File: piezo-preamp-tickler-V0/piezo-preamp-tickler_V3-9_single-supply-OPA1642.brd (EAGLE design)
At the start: 100 x 20 mm, 61 parts, among them IC1 OPA1642, IC2 MCP73831, IC3 QS6K1, IC4 BQ297X, IC5 SC4503, IC6 TPS7A49, J1 HEADPHONES, J2 PHONE, J3 Mixer, J5 Battery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

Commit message: resolved cosmetic issues in mems and piezo for 5k and 50k resistor values that should be 4.7k and 47K
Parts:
- R13: value 5k -> 4.7K
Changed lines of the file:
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@@
 <attribute name="VALUE" x="72.797" y="12.941" size="0.6604" layer="27" font="vector" ratio="15" rot="R180"/>
 </element>
-<element name="R13" library="CMU-ArtFab" package="R0603" value="5k" x="65.375" y="10.115" smashed="yes">
+<element name="R13" library="CMU-ArtFab" package="R0603" value="4.7K" x="65.375" y="10.115" smashed="yes">
 <attribute name="NAME" x="66.14" y="11.405" size="0.6604" layer="25" font="vector" ratio="15" rot="R180"/>
 <attribute name="VALUE" x="64.65" y="8.771" size="0.6604" layer="27" font="vector" ratio="15"/>

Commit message: capacitors renumbered in sequence
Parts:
- C10: value 2.2pF -> 56nF
- C11: value 68uF -> 2.2pF; device rcl:C1206 -> rcl:C0603
- C12: value 10uF -> 68uF; device rcl:C0603 -> rcl:C1206
- C13: value 10nF -> 10uF
- C15: value 10uF -> 10nF
- C16: value 4.7uF -> 10uF
- C7: value 0.1uF -> 4.7uF
- C8: value 10uF -> 0.1uF
- C9: value 56nF -> 10uF
- moved C9 29.1 mm to (47.4, 11.6)
- moved C11 28.4 mm to (79.2, 6.31), turned to 0 degrees
- moved C8 28.1 mm to (75.0, 6.30)
- moved C12 18.5 mm to (52.3, 15.2)
- moved C7 16.0 mm to (59.1, 7.80)
- moved C16 13.9 mm to (68.6, 18.0), turned to 180 degrees
- moved C14 13.1 mm to (70.5, 6.32), turned to 180 degrees
- moved C13 6.49 mm to (65.5, 2.23)
- moved C10 5.83 mm to (75.0, 2.32)
- moved C15 3.98 mm to (64.6, 18.0), turned to 0 degrees
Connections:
- net +12V: now also C14.1; no longer C12.1
- net BATGND: now also C8.1; no longer C7.1
- net GND: now also C10.2, C13.2, C16.2; no longer C11.2, C14.2, C8.2
- net N$26: now also C14.2; no longer C13.2
- net N$28: now also C15.1; no longer C14.1
- net N$29: now also C10.1; no longer C9.1
- net N$30: now also C11.2; no longer C10.2
- net N$42: now also C8.2; no longer C7.2
- net USBGND: now also C7.2; no longer C16.2
- net V+: now also C12.1, C16.1; no longer C10.1, C15.1
- net VBAT: now also C7.1, C9.1; no longer C16.1, C8.1

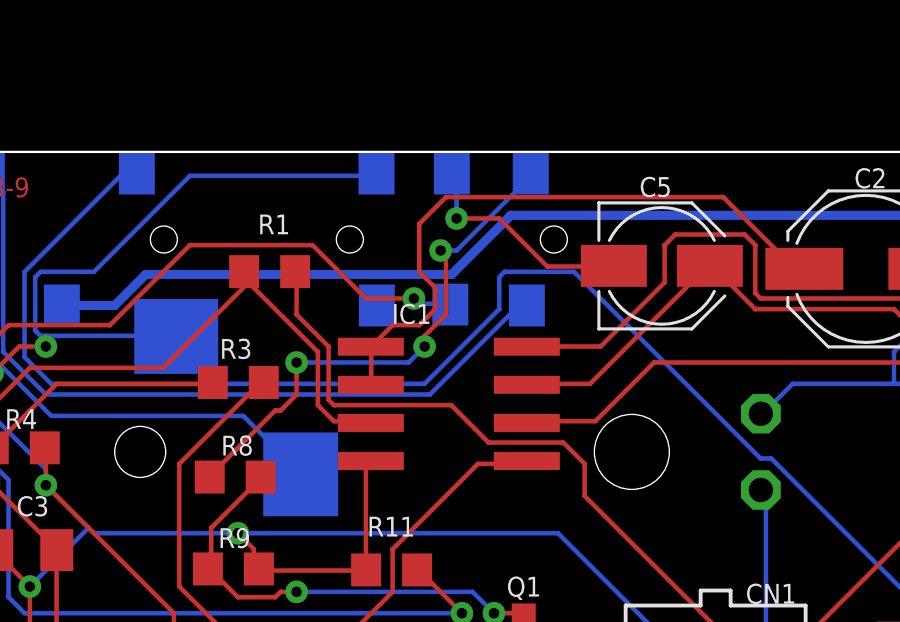
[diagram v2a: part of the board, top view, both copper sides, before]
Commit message: OPA1642 device added from CMU artfab library
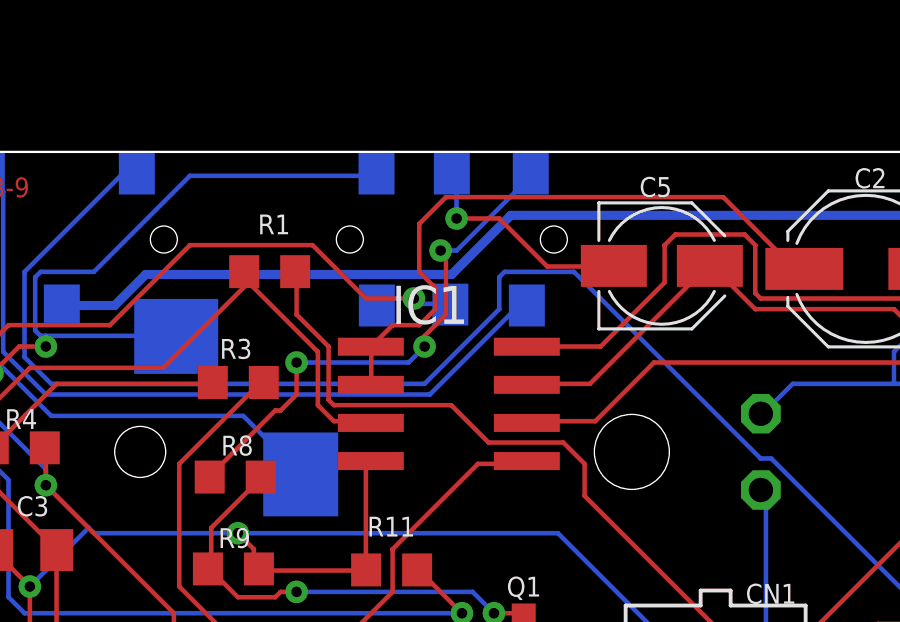
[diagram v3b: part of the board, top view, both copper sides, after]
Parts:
- IC1: device linear:SO08 -> CMU-ArtFab:SO08
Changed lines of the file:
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@@
 <attribute name="VALUE" x="58.065" y="6.495" size="0.6604" layer="27" font="vector" ratio="15"/>
-</element>
-<element name="IC1" library="linear" library_urn="urn:adsk.eagle:library:262" package="SO08" package3d_urn="urn:adsk.eagle:package:16404/2" value="OPA1642" x="20.9" y="11.6" smashed="yes" rot="R270">
-<attribute name="NAME" x="18.995" y="14.267" size="0.6604" layer="25" font="vector" ratio="15"/>
-<attribute name="VALUE" x="19.195" y="8.263" size="0.6604" layer="27" font="vector" ratio="15"/>
 </element>
 <element name="C5" library="resistor" library_urn="urn:adsk.eagle:library:348" package="PANASONIC_B" package3d_urn="urn:adsk.eagle:package:25911/1" value="10uF" x="28" y="16.2" smashed="yes">
@@
 <attribute name="VALUE" x="36.55" y="13.275" size="0.6604" layer="27" font="vector" ratio="15" rot="R180"/>
 </element>
+<element name="IC1" library="CMU-ArtFab" package="SO08" package3d_urn="urn:adsk.eagle:package:16404/2" value="OPA1642" x="20.9" y="11.6" rot="R270"/>
 </elements>
 <signals>
@@
 <contactref element="J1" pad="RING2"/>
 <contactref element="J2" pad="RING2"/>
-<contactref element="IC1" pad="4"/>
 <wire x1="3.3782" y1="1.4224" x2="2.1336" y2="2.667" width="0.1524" layer="1"/>
 <wire x1="6.7564" y1="1.4224" x2="3.3782" y2="1.4224" width="0.1524" layer="1"/>
@@
 <wire x1="18.1356" y1="9.6012" x2="18.1356" y2="6.223" width="0.1524" layer="1"/>
 <wire x1="18.1356" y1="6.223" x2="18.142" y2="6.066" width="0.1524" layer="1"/>
-<wire x1="18.1356" y1="9.6012" x2="18.3" y2="9.695" width="0.1524" layer="1"/>
 <wire x1="18.1356" y1="6.0452" x2="14.5796" y2="6.0452" width="0.1524" layer="1"/>
 <wire x1="14.5796" y1="6.0452" x2="14.569" y2="6.1" width="0.1524" layer="1"/>
@@
 <via x="77.6986" y="4.8006" extent="1-16" drill="0.35"/>
 <via x="89.9668" y="13.335" extent="1-16" drill="0.35"/>
+<contactref element="IC1" pad="4"/>
+<wire x1="18.1356" y1="9.6012" x2="18.3" y2="9.695" width="0.1524" layer="1"/>
 </signal>
 <signal name="N$5">
 <contactref element="R7" pad="1"/>
-<contactref element="IC1" pad="5"/>
 <wire x1="16.002" y1="2.3114" x2="15.6464" y2="2.3114" width="0.1524" layer="1"/>
 <wire x1="19.0246" y1="5.334" x2="16.002" y2="2.3114" width="0.1524" layer="1"/>
@@
 <wire x1="23.4696" y1="9.6012" x2="21.8694" y2="9.6012" width="0.1524" layer="1"/>
 <wire x1="15.6464" y1="2.3114" x2="15.489" y2="2.305" width="0.1524" layer="1"/>
+<contactref element="IC1" pad="5"/>
 <wire x1="23.4696" y1="9.6012" x2="23.5" y2="9.695" width="0.1524" layer="1"/>
 </signal>
 <signal name="N$6">
 <contactref element="R6" pad="P$2"/>
-<contactref element="IC1" pad="7"/>
 <contactref element="C5" pad="+"/>
 <wire x1="25.6032" y1="12.2682" x2="23.6474" y2="12.2682" width="0.1524" layer="1"/>
 <wire x1="29.5148" y1="16.1798" x2="25.6032" y2="12.2682" width="0.1524" layer="1"/>
-<wire x1="23.6474" y1="12.2682" x2="23.5" y2="12.235" width="0.1524" layer="1"/>
 <wire x1="29.5148" y1="16.1798" x2="29.6" y2="16.2" width="0.1524" layer="1"/>
 <wire x1="47.4726" y1="8.5344" x2="49.4284" y2="8.5344" width="0.1524" layer="1"/>
@@
 <wire x1="49.4284" y1="8.5344" x2="49.6" y2="8.5" width="0.1524" layer="1"/>
 <wire x1="29.6926" y1="16.1798" x2="29.6" y2="16.2" width="0.1524" layer="1"/>
+<contactref element="IC1" pad="7"/>
+<wire x1="23.6474" y1="12.2682" x2="23.5" y2="12.235" width="0.1524" layer="1"/>
 </signal>
 <signal name="N$7">
 <contactref element="R5" pad="2"/>
 <contactref element="R6" pad="P$3"/>
-<contactref element="IC1" pad="6"/>
 <wire x1="44.0944" y1="14.5796" x2="41.6052" y2="17.0688" width="0.1524" layer="1"/>
 <wire x1="47.4726" y1="14.5796" x2="44.0944" y2="14.5796" width="0.1524" layer="16"/>
@@
 <wire x1="42.4942" y1="12.9794" x2="36.449" y2="12.9794" width="0.1524" layer="16"/>
 <wire x1="44.0944" y1="14.5796" x2="42.4942" y2="12.9794" width="0.1524" layer="16"/>
-<wire x1="23.6474" y1="11.0236" x2="23.5" y2="10.965" width="0.1524" layer="1"/>
 <via x="44.0944" y="14.5796" extent="1-16" drill="0.35"/>
 <via x="36.449" y="12.9794" extent="1-16" drill="0.35"/>
+<contactref element="IC1" pad="6"/>
+<wire x1="23.6474" y1="11.0236" x2="23.5" y2="10.965" width="0.1524" layer="1"/>
 </signal>
 <signal name="N$10">
@@
 </signal>
 <signal name="N$24">
-<contactref element="IC1" pad="2"/>
-<contactref element="IC1" pad="1"/>
 <contactref element="C2" pad="+"/>
-<wire x1="18.3134" y1="13.335" x2="18.3134" y2="12.2682" width="0.1524" layer="1"/>
-<wire x1="18.3134" y1="12.2682" x2="18.3" y2="12.235" width="0.1524" layer="1"/>
-<wire x1="18.3134" y1="13.335" x2="18.3" y2="13.505" width="0.1524" layer="1"/>
 <wire x1="32.3596" y1="16.1798" x2="32.7152" y2="16.1798" width="0.1524" layer="1"/>
 <wire x1="30.0482" y1="18.4912" x2="32.3596" y2="16.1798" width="0.1524" layer="1"/>
@@
 <wire x1="18.3134" y1="13.5128" x2="19.0246" y2="14.224" width="0.1524" layer="1"/>
 <wire x1="32.7152" y1="16.1798" x2="32.75" y2="16.1" width="0.1524" layer="1"/>
+<contactref element="IC1" pad="2"/>
+<contactref element="IC1" pad="1"/>
+<wire x1="18.3134" y1="13.335" x2="18.3134" y2="12.2682" width="0.1524" layer="1"/>
+<wire x1="18.3134" y1="12.2682" x2="18.3" y2="12.235" width="0.1524" layer="1"/>
+<wire x1="18.3134" y1="13.335" x2="18.3" y2="13.505" width="0.1524" layer="1"/>
 <wire x1="18.3134" y1="13.5128" x2="18.3" y2="13.505" width="0.1524" layer="1"/>
 </signal>
@@
 <contactref element="R2" pad="2"/>
 <contactref element="D1" pad="2"/>
-<contactref element="IC1" pad="3"/>
 <wire x1="4.2672" y1="2.4892" x2="4.9784" y2="2.4892" width="0.1524" layer="1"/>
 <wire x1="4.9784" y1="2.4892" x2="6.0452" y2="2.4892" width="0.1524" layer="1"/>
@@
 <wire x1="18.1356" y1="11.0236" x2="17.0688" y2="11.0236" width="0.1524" layer="1"/>
 <wire x1="14.224" y1="16.002" x2="14.077" y2="16.008" width="0.1524" layer="1"/>
-<wire x1="18.1356" y1="11.0236" x2="18.3" y2="10.965" width="0.1524" layer="1"/>
 <wire x1="4.9784" y1="9.4234" x2="4.9784" y2="2.4892" width="0.1524" layer="1"/>
 <wire x1="4.8006" y1="9.6012" x2="4.9784" y2="9.4234" width="0.1524" layer="1"/>
@@
 <wire x1="14.224" y1="15.6464" x2="11.3792" y2="12.8016" width="0.1524" layer="1"/>
 <wire x1="14.224" y1="15.6464" x2="14.077" y2="16.008" width="0.1524" layer="1"/>
+<contactref element="IC1" pad="3"/>
+<wire x1="18.1356" y1="11.0236" x2="18.3" y2="10.965" width="0.1524" layer="1"/>
 </signal>
 <signal name="N$8">
@@
 <contactref element="R3" pad="2"/>
 <contactref element="L1" pad="2"/>
-<contactref element="IC1" pad="8"/>
 <wire x1="11.9126" y1="9.6012" x2="14.5796" y2="12.2682" width="0.1524" layer="1"/>
 <wire x1="11.9126" y1="5.5118" x2="11.9126" y2="9.6012" width="0.1524" layer="1"/>
@@
 <wire x1="41.783" y1="15.113" x2="31.2928" y2="15.113" width="0.1524" layer="1"/>
 <wire x1="43.561" y1="13.335" x2="41.783" y2="15.113" width="0.1524" layer="1"/>
+<wire x1="43.561" y1="13.335" x2="43.685" y2="13.284" width="0.1524" layer="1"/>
+<contactref element="IC1" pad="8"/>
 <wire x1="23.6474" y1="13.5128" x2="23.5" y2="13.505" width="0.1524" layer="1"/>
-<wire x1="43.561" y1="13.335" x2="43.685" y2="13.284" width="0.1524" layer="1"/>
 </signal>
 <signal name="N$9">
